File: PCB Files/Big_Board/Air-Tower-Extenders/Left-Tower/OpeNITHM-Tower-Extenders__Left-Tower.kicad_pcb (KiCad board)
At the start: 2 copper layers, 26.4 x 34.6 mm, 6 parts, among them J1 Conn_01x04_Male, J2 Conn_01x04_Male, J3 Conn_01x09_Male, J4 Conn_01x09_Male

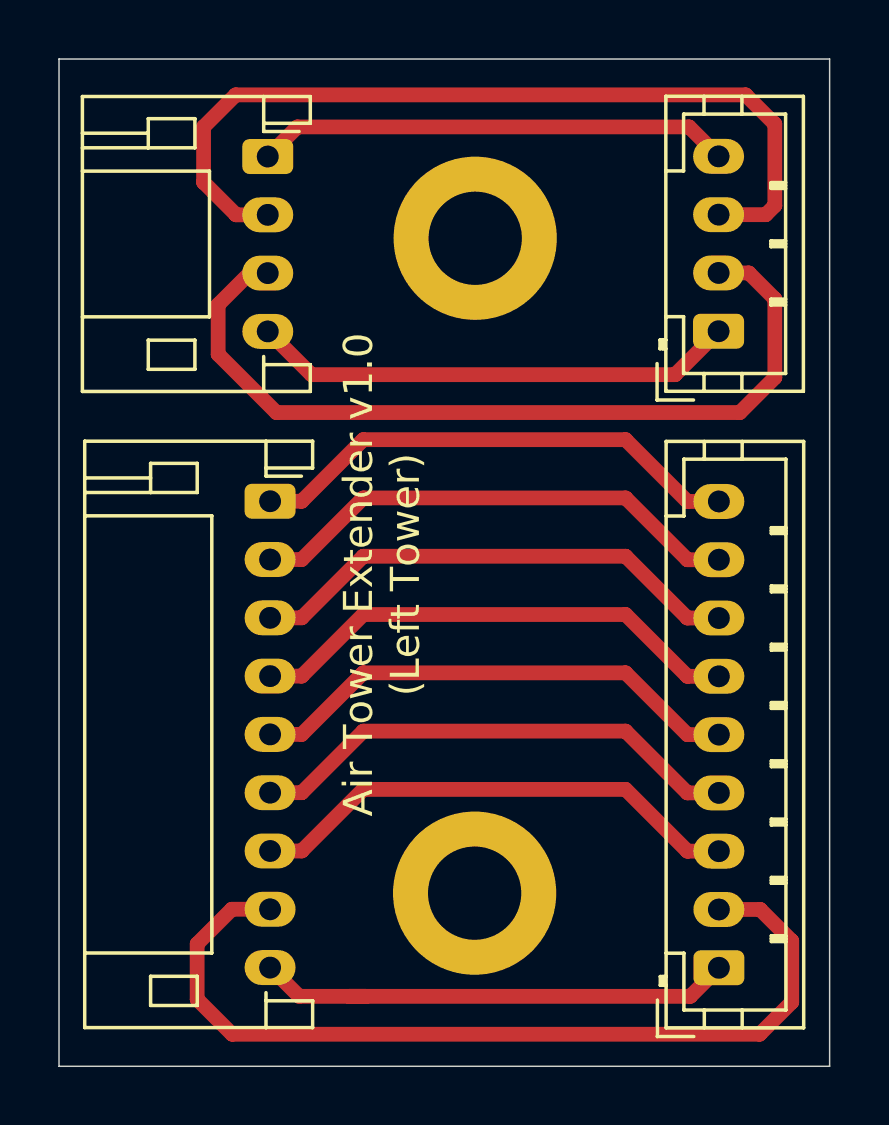
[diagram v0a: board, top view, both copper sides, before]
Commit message: Update the gerbers for the air extender PCBs
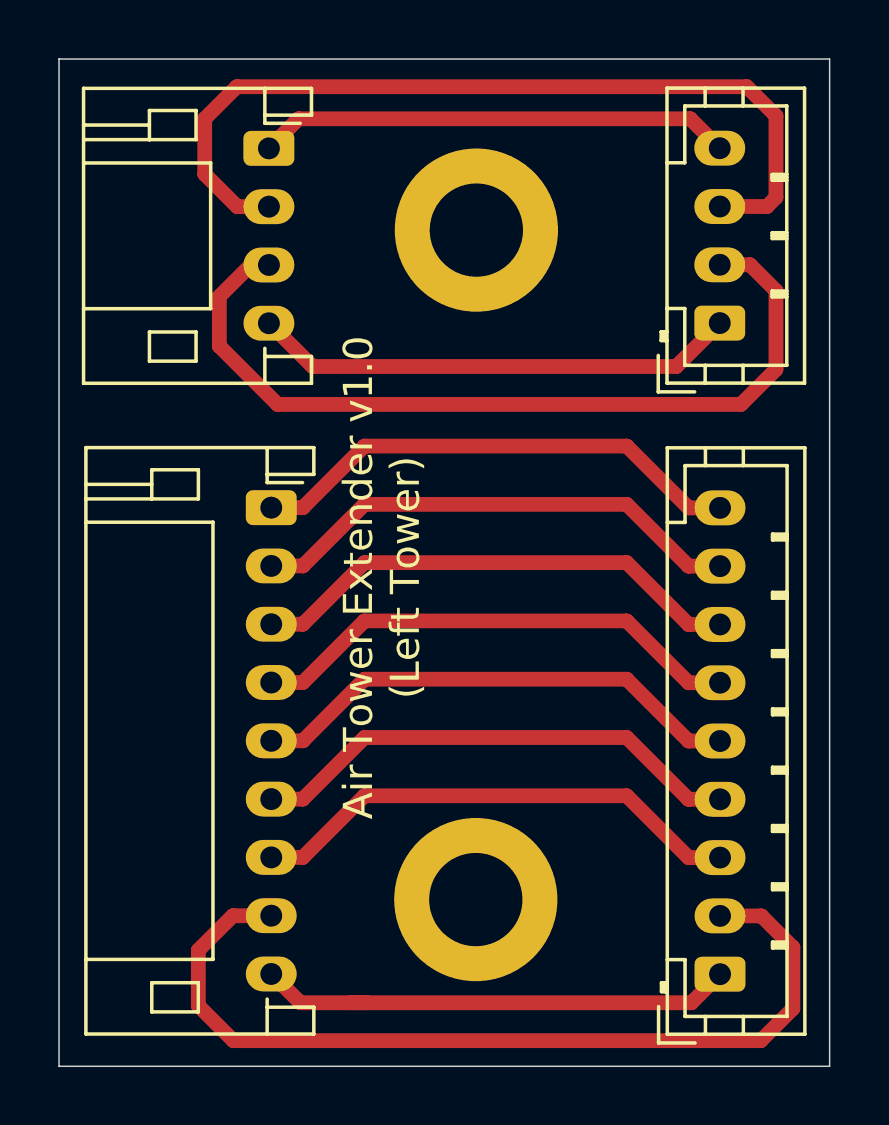
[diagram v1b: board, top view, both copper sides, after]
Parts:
- moved J1 0.28 mm to (66.8, 47.0)
- moved J2 0.28 mm to (82.2, 53.0)
- moved H1 0.28 mm to (73.9, 49.8)
- moved H2 0.22 mm to (73.9, 72.8)
- moved J3 0.22 mm to (66.8, 59.3)
- moved J4 0.22 mm to (82.2, 75.3)
